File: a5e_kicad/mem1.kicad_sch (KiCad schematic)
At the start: 59 parts, among them U1301 IS43LQ32256A-062BLI

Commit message: add vias to lppdr balls
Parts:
- renumbered C1301 to C41, C1315 to C42, C1343 to C43, C1329 to C44, C1302 to C45, C1316 to C46, C1344 to C47, C1330 to C48, C1303 to C49, C1317 to C50, C1345 to C51, C1331 to C52, C1304 to C53, C1318 to C54, C1346 to C55, C1332 to C56, C1305 to C57, C1319 to C58, C1347 to C59, C1333 to C60, C1306 to C61, C1320 to C62, C1348 to C63, C1334 to C64, C1307 to C65, C1321 to C66, C1349 to C67, C1335 to C68, C1308 to C69, C1322 to C70, C1350 to C71, C1336 to C72, C1309 to C73, C1323 to C74, C1351 to C75, C1337 to C76, C1310 to C77, C1324 to C78, C1352 to C79, C1338 to C80, C1311 to C81, C1325 to C82, C1353 to C83, C1339 to C84, C1312 to C85, C1326 to C86, C1354 to C87, C1340 to C88, C1313 to C89, C1327 to C90, C1355 to C91, C1341 to C92, C1314 to C93, C1328 to C94, C1356 to C95, C1342 to C96, R1301 to R43, R1304 to R44, U1301 to U12

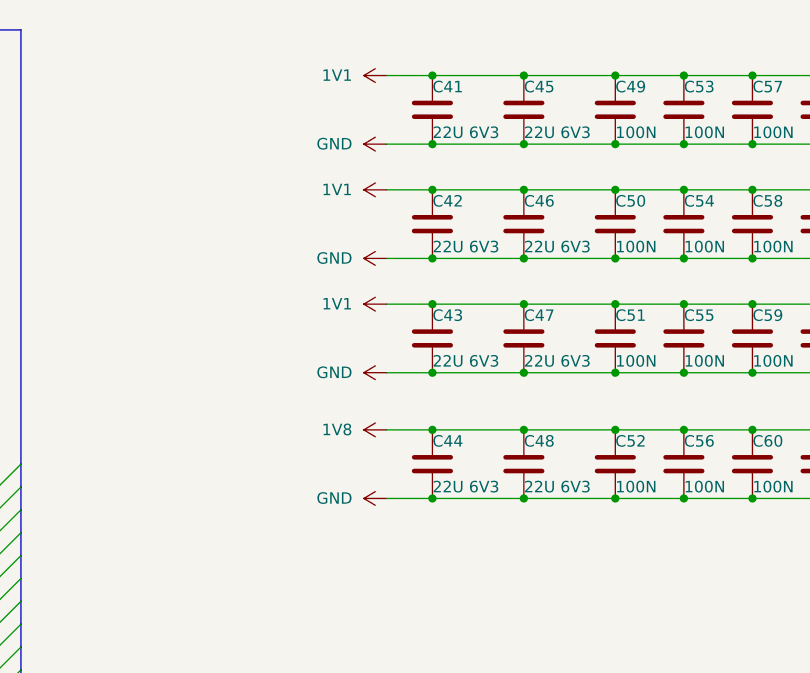
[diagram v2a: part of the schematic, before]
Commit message: remove hyperram and add lpddr4 bypass caps
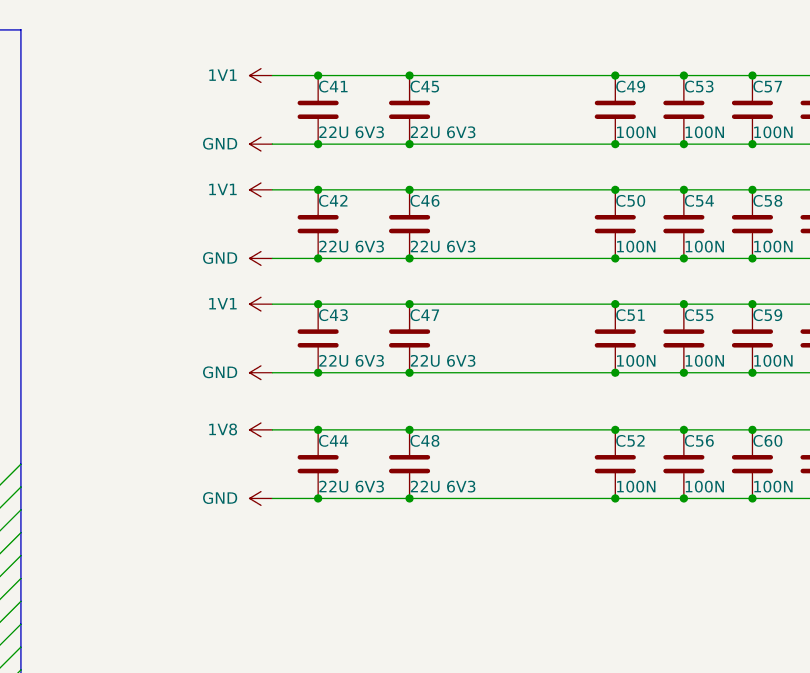
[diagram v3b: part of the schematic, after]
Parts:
- C49, C50, C51, C52, C53, C54, C55, C56, C57, C58, C59, C60, C61, C62, C63, C64, C65, C66, C67, C68, C69, C70, C71, C72, C73, C74, C75, C76, C77, C78, C79, C80, C81, C82, C83, C84, C85, C86, C87, C88, C89, C90, C91, C92, C93, C94, C95, C96: footprint Capacitor_SMD:C_0402_1005Metric -> Capacitor_SMD:C_0201_0603Metric
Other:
- moved on the sheet: C41, C42, C43, C44, C45, C46, C47, C48

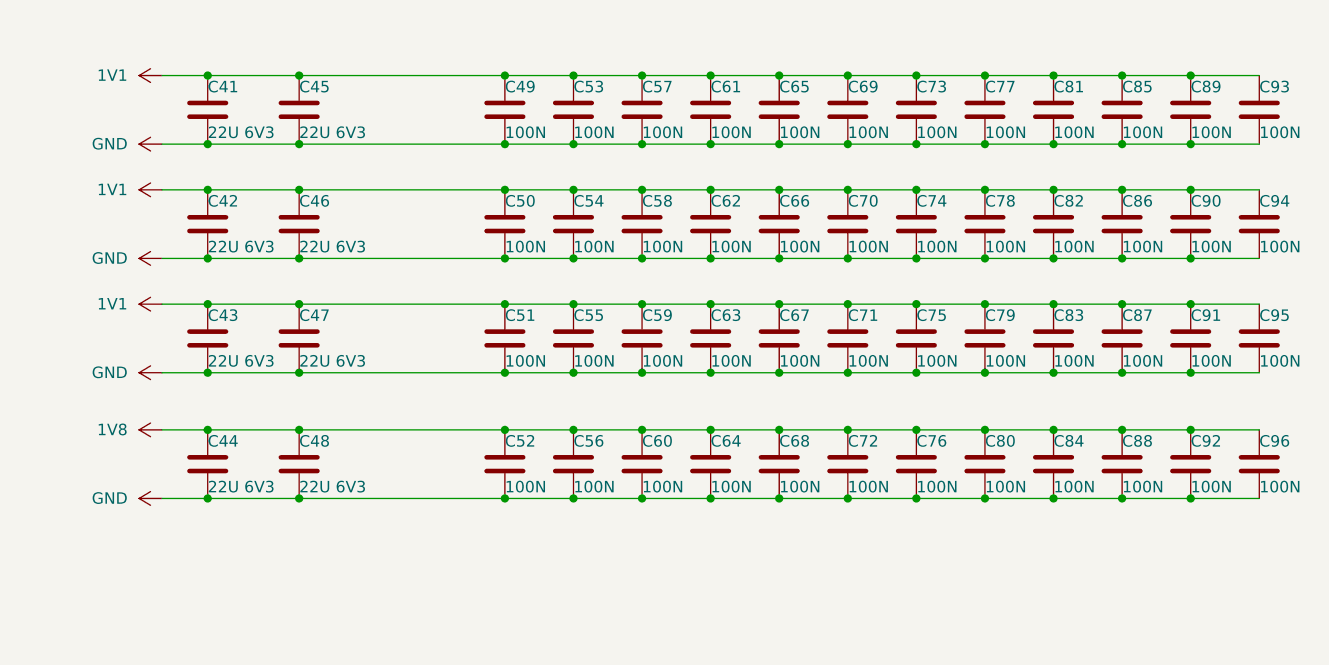
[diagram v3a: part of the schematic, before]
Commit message: remove extra components and make 1v8 plane
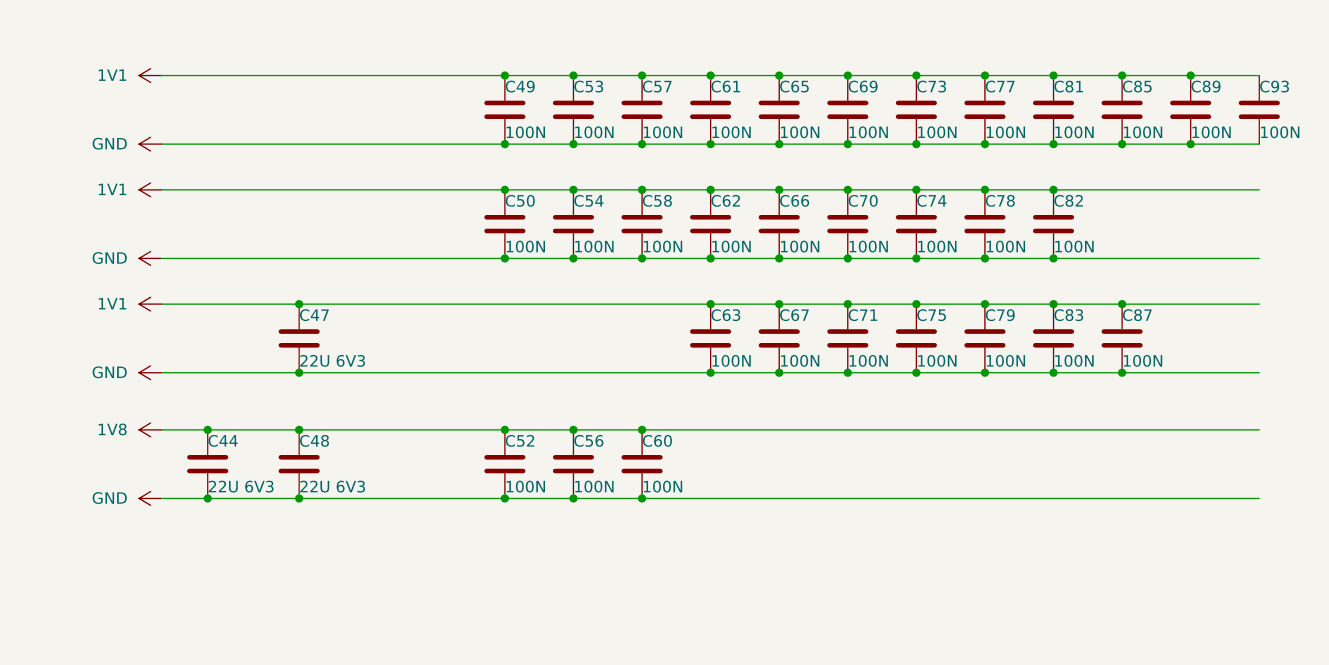
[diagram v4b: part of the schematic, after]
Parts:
- removed C41, C42, C43, C45, C46: 22U 6V3, Capacitor_SMD:C_0402_1005Metric, symbol Device:C
- removed C51, C55, C59, C64, C68, C72, C76, C80, C84, C86, C88, C90, C91, C92, C94, C95, C96: 100N, Capacitor_SMD:C_0201_0603Metric, symbol Device:C
